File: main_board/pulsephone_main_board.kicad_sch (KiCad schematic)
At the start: 94 parts, among them J1 USB_C_Receptacle_USB2.0_14P, J2 Conn_01x05, J3 Conn_2Rows-35Pins_MountingPin, J4 Conn_2Rows-35Pins_MountingPin, J5 Conn_2Rows-35Pins_MountingPin, J6 Conn_01x01_Socket, J7 Micro_SD_Card_Det1, U1 AP2112K-3.3, U2 PCM5102APWR, U4 TPS63020DSJR/3.7V Reg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

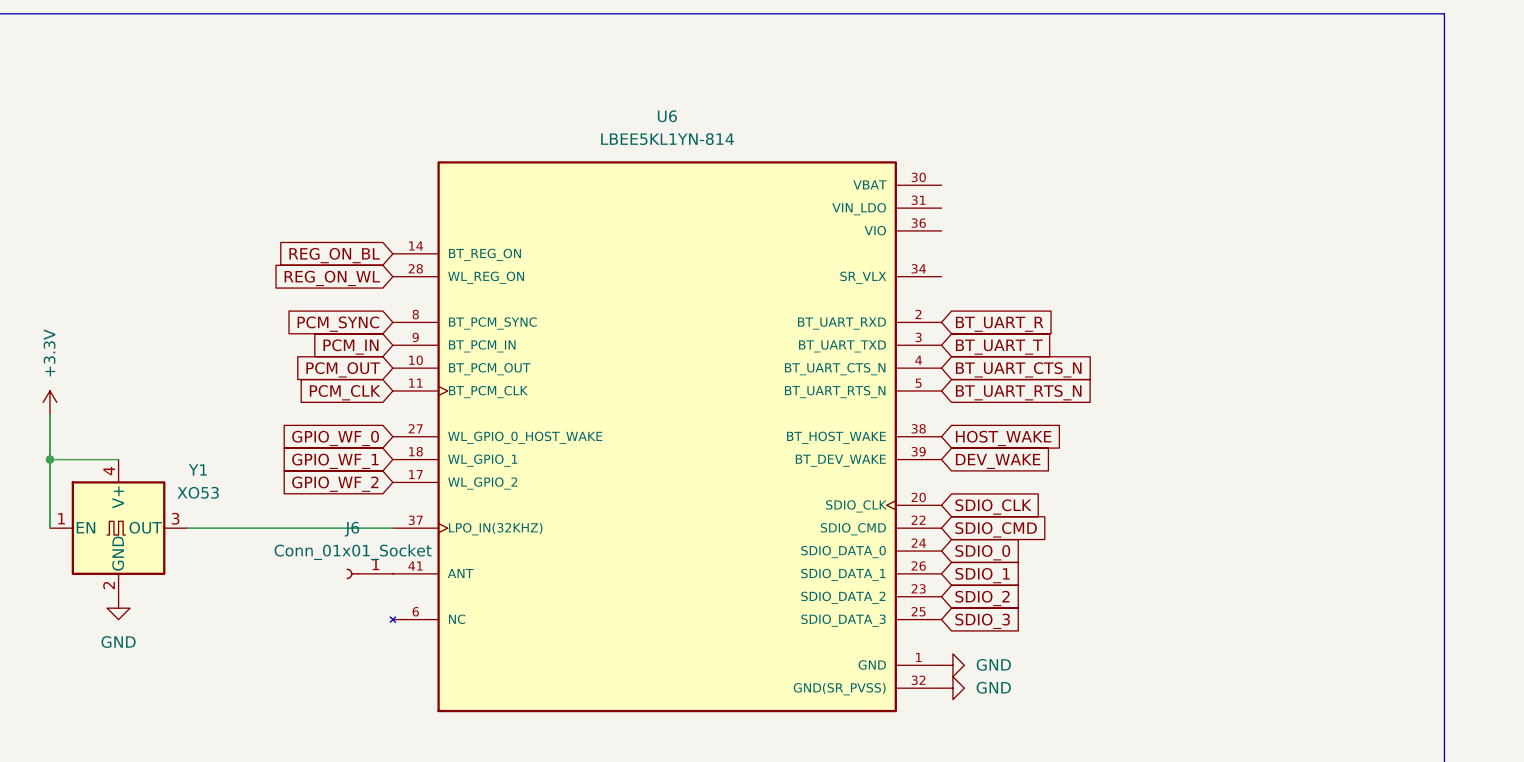
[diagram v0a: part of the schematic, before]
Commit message: Rev2: fix LBEE5KL1YN power pins, SR_VLX inductor, Y1 LPO_IN wiring, DRC constraints
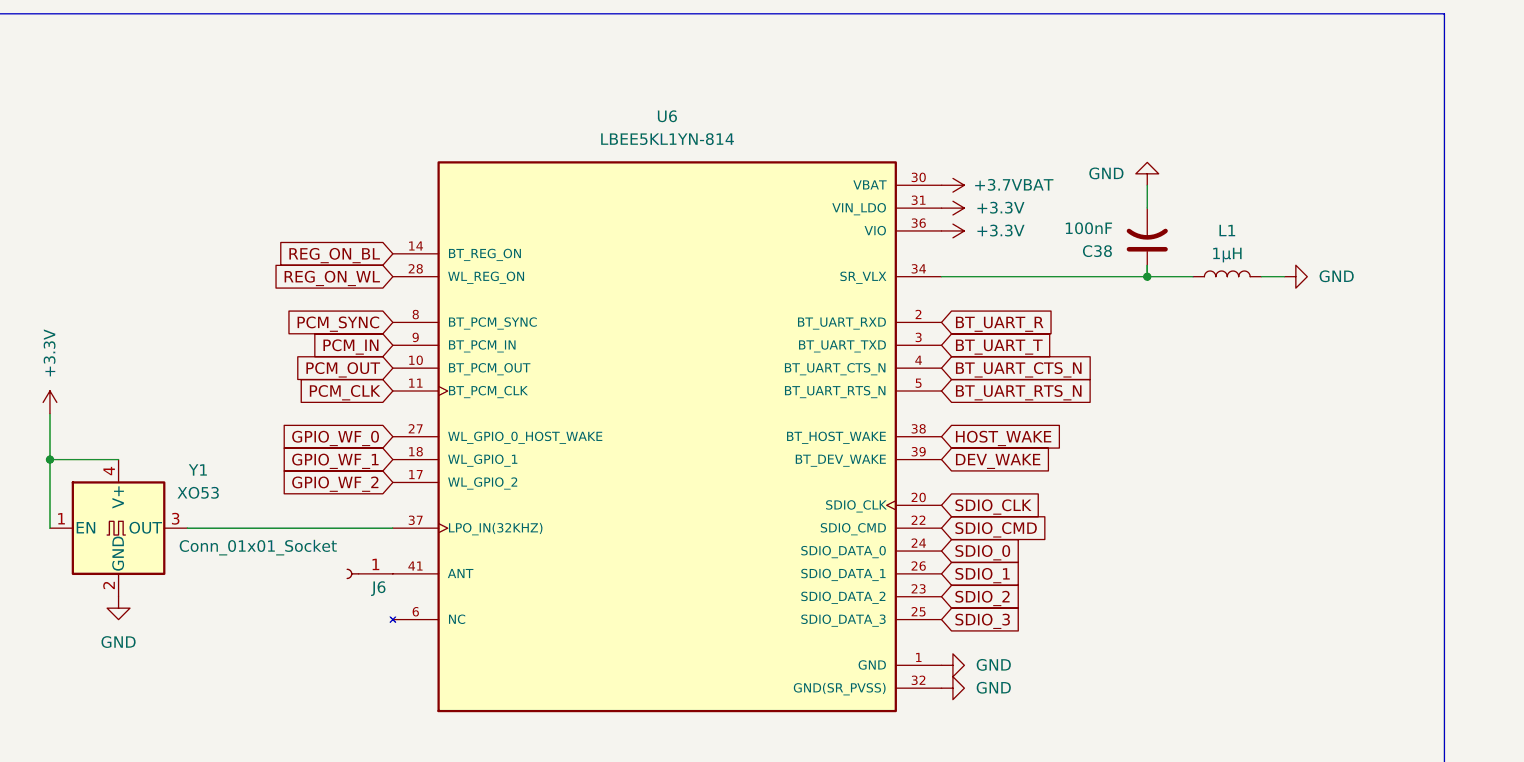
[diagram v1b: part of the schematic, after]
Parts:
- added C38: 100nF, Capacitor_SMD:C_0805_2012Metric, symbol Device:C_US
- added L1: 1µH, Inductor_SMD:L_01005_0402Metric, symbol Device:L
- U3: value ~ -> (none)
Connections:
- net +3.3V: now also U6.31 (VIN_LDO), U6.36 (VIO)
- net +3.7VBAT: now also U6.30 (VBAT)
- net GND: now also C38.2, L1.2
- net at U6.34 (SR_VLX): now also C38.1, L1.1

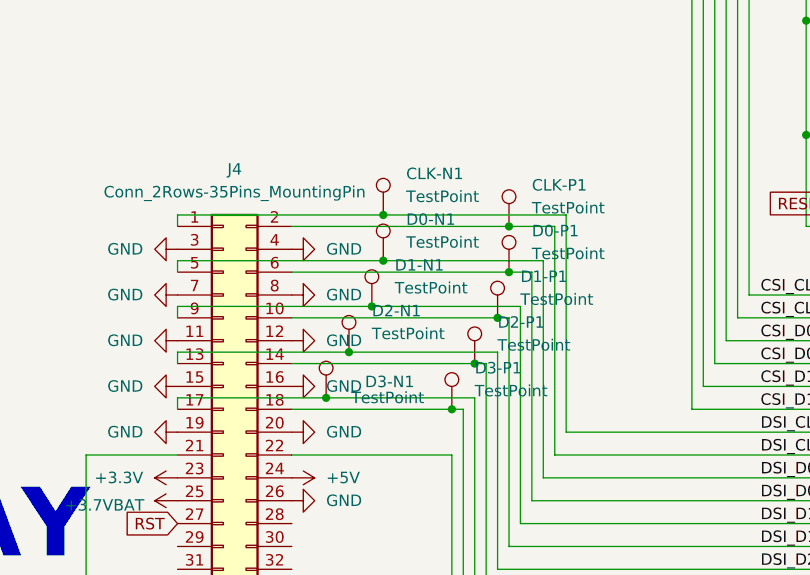
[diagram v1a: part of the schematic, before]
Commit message: Rev2: GND copper pour, reroute, power trace widths
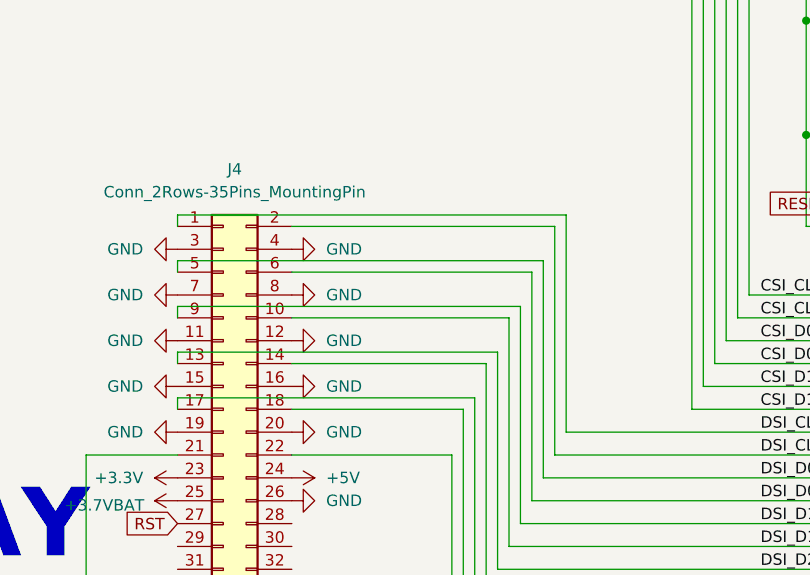
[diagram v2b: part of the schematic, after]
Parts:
- removed CLK-N1, CLK-P1, D0-N1, D0-P1, D1-N1, D1-P1, D2-N1, D2-P1, D3-N1, D3-P1: TestPoint, TestPoint:TestPoint_Pad_D2.5mm, symbol Connector:TestPoint

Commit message: new WIP mod port (new connector for additional modules to further modify the phone
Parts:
- added F1, F2: PPTC, symbol Device:Polyfuse_Small
- added J8: Conn_2Rows-35Pins_MountingPin, DF40-34P:HIROSE_DF40C-34DS-0.4V_58_, symbol Connector_Generic_MountingPin:Conn_2Rows-35Pins_MountingPin
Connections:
- net +3.3V: now also F1.1
- net +3.7VBAT: now also F2.2
- net GND: now also J8.1 (Pin_1), J8.2 (Pin_2), J8.31 (Pin_31), J8.32 (Pin_32), J8.33 (Pin_33), J8.34 (Pin_34)
- new net: F1.2, J8.3 (Pin_3)
- new net: F2.1, J8.4 (Pin_4)
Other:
- note added: "MOD PORT"
- moved on the sheet: 3.3V1, 5V1, BT1, C1, C10, C11, C12, C13, C33, C34, C35, C36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

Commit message: new modport addition to pcb -- 3 unconnected pins, WIP
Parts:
- F1, F2: footprint (none) -> Resistor_SMD:R_0805_2012Metric
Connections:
- net BT_UART_R: now also MCM93_MOD1.103 (33); no longer MCM93_MOD1.102 (32)
- net BT_UART_T: now also MCM93_MOD1.102 (32); no longer MCM93_MOD1.103 (33)
- net CSI_D0_N: now also J3.6 (Pin_6); no longer J3.5 (Pin_5)
- net CSI_D0_P: now also J3.5 (Pin_5); no longer J3.6 (Pin_6)
- net CSI_D1_N: now also J3.10 (Pin_10); no longer J3.9 (Pin_9)
- net CSI_D1_P: now also J3.9 (Pin_9); no longer J3.10 (Pin_10)
- net MOD_GPIO_95: now reaches MCM93_MOD1.95 (25)
- net MOD_GPIO_95: now also J8.13 (Pin_13)
- net MOD_GPIO_96: now reaches MCM93_MOD1.96 (26)
- net MOD_GPIO_96: now also J8.14 (Pin_14)
- net MOD_GPIO_99: now reaches MCM93_MOD1.99 (29)
- net MOD_GPIO_99: now also J8.15 (Pin_15)
- net MOD_UART6_RTS: now reaches MCM93_MOD1.106 (1)
- net MOD_UART6_RTS: now also J8.7 (Pin_7)
- net MOD_UART6_CTS: now reaches MCM93_MOD1.107 (2)
- net MOD_UART6_CTS: now also J8.8 (Pin_8)
- net MOD_GPIO_115: now reaches MCM93_MOD1.115 (10)
- net MOD_GPIO_115: now also J8.16 (Pin_16)
- net MOD_GPIO_116: now reaches MCM93_MOD1.116 (11)
- net MOD_GPIO_116: now also J8.17 (Pin_17)
- net MOD_GPIO_117: now reaches MCM93_MOD1.117 (12)
- net MOD_GPIO_117: now also J8.18 (Pin_18)
- net MOD_GPIO_118: now reaches MCM93_MOD1.118 (13)
- net MOD_GPIO_118: now also J8.19 (Pin_19)
- net MOD_GPIO_119: now reaches MCM93_MOD1.119 (14)
- net MOD_GPIO_119: now also J8.20 (Pin_20)
- net MOD_GPIO_120: now reaches MCM93_MOD1.120 (15)
- net MOD_GPIO_120: now also J8.21 (Pin_21)
- net MOD_I2C7_SCL: now reaches MCM93_MOD1.121 (16)
- net MOD_I2C7_SCL: now also J8.9 (Pin_9)
- net MOD_I2C8_SDA: now reaches MCM93_MOD1.122 (17)
- net MOD_I2C8_SDA: now also J8.10 (Pin_10)
- net MOD_I2C8_SCL: now reaches MCM93_MOD1.123 (18)
- net MOD_I2C8_SCL: now also J8.11 (Pin_11)
- net MOD_UART6_RX: now reaches MCM93_MOD1.124 (19)
- net MOD_UART6_RX: now also J8.5 (Pin_5)
- net MOD_UART6_TX: now reaches MCM93_MOD1.125 (20)
- net MOD_UART6_TX: now also J8.6 (Pin_6)
- net MOD_GPIO_128: now reaches MCM93_MOD1.128 (23)
- net MOD_GPIO_128: now also J8.22 (Pin_22)
- net MOD_GPIO_130: now reaches MCM93_MOD1.130 (25)
- net MOD_GPIO_130: now also J8.23 (Pin_23)
- net MOD_GPIO_48: now reaches J8.12 (Pin_12)
- net MOD_GPIO_48: now also MCM93_MOD1.48 (13)

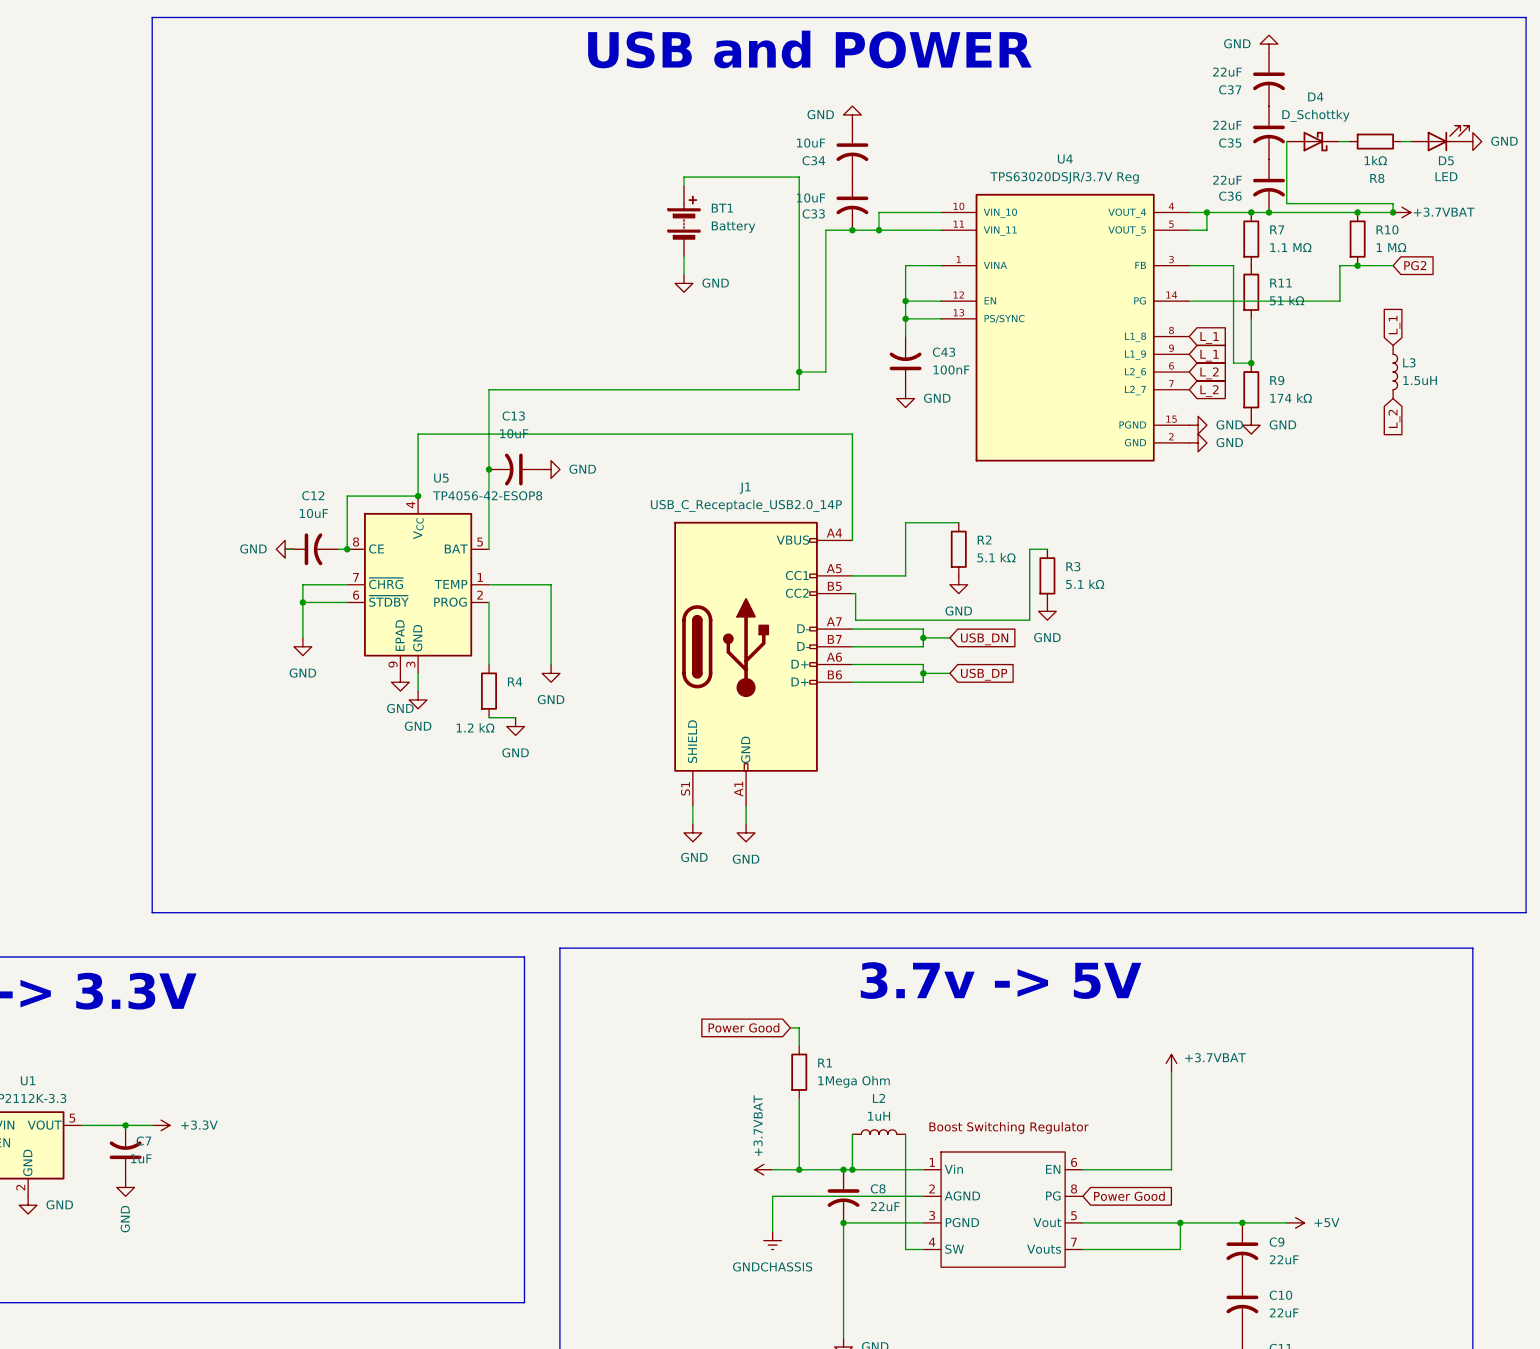
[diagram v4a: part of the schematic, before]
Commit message: add power good leds to 5v and 3v3.
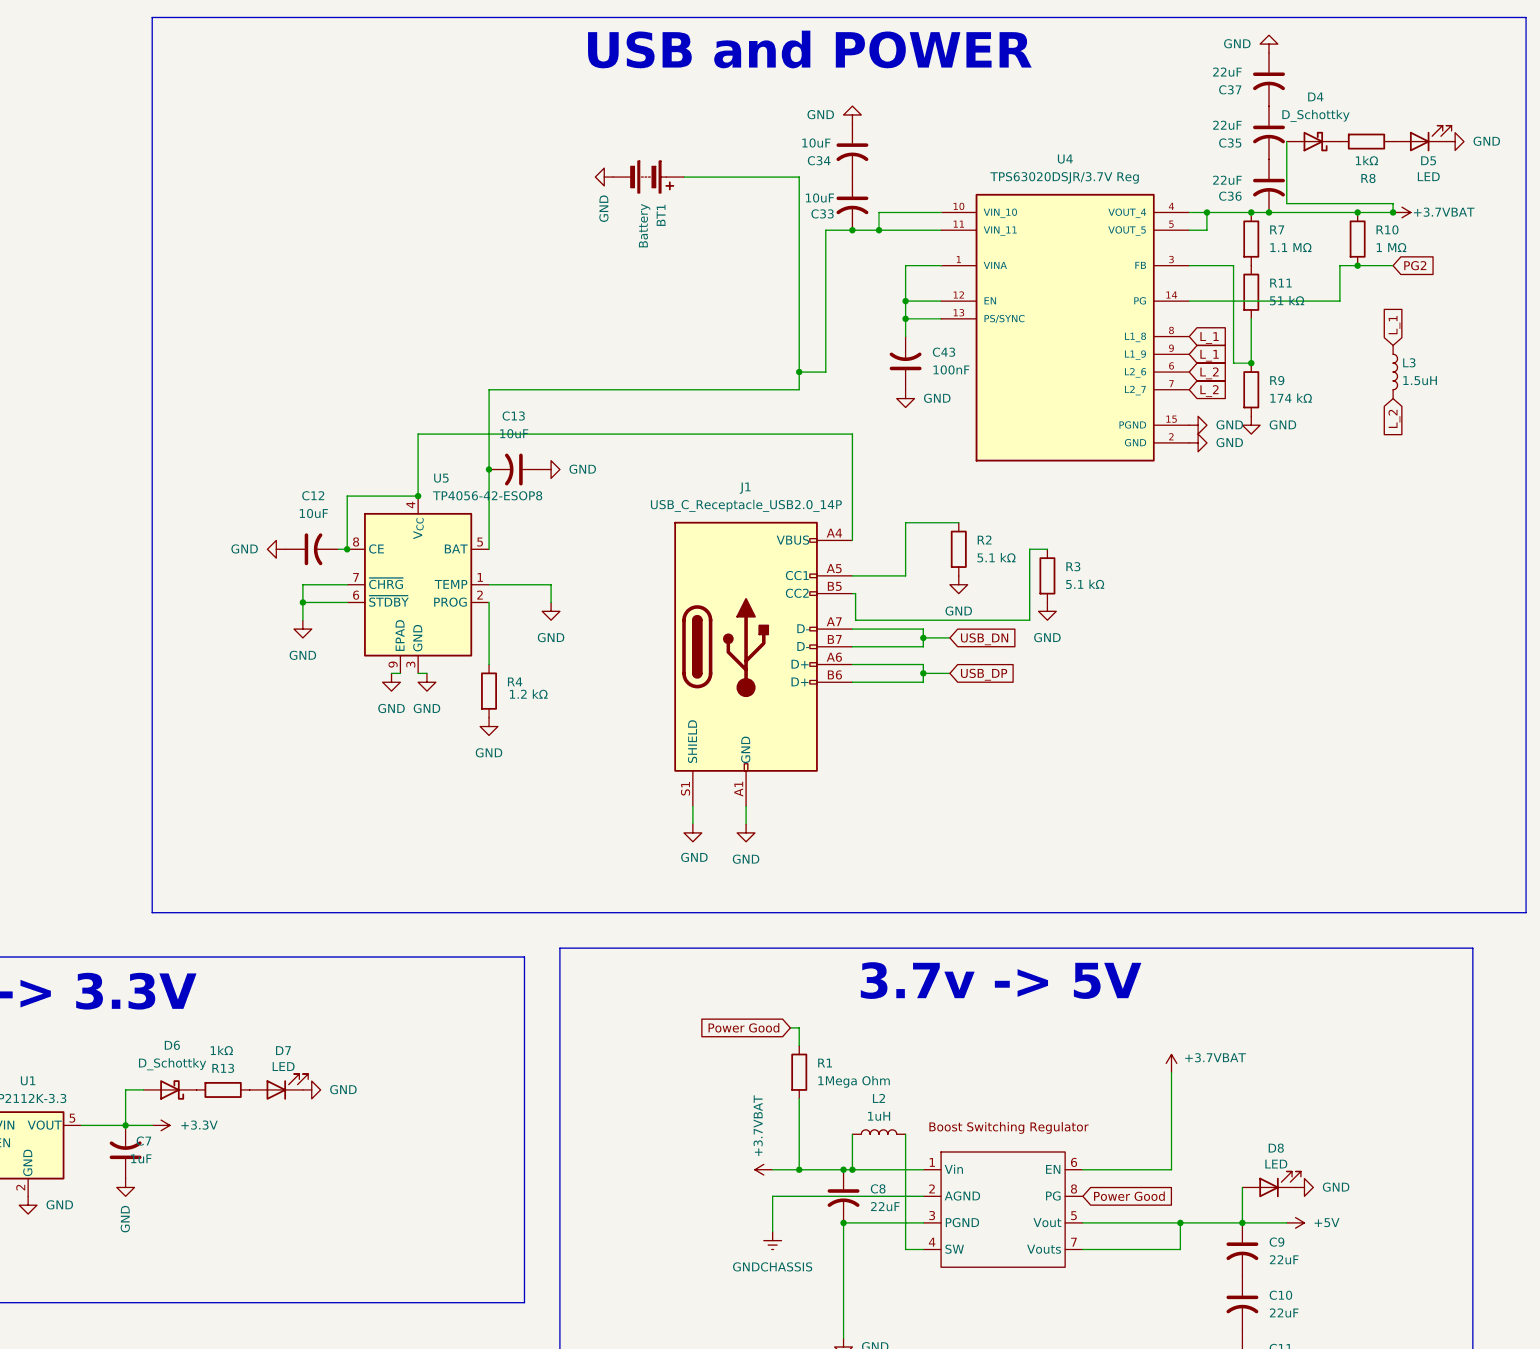
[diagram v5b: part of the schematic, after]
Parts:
- added D6: D_Schottky, Diode_SMD:D_SMA, symbol Device:D_Schottky
- added D7, D8: LED, LED_SMD:LED_0805_2012Metric, symbol Device:LED
- added R13: 1kΩ, Resistor_SMD:R_0805_2012Metric, symbol Device:R
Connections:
- net +3.3V: now also D6.2 (A)
- net +5V: now also D8.2 (A)
- net GND: now also D7.1 (K), D8.1 (K)
- new net: D7.2 (A), R13.1
- new net: D6.1 (K), R13.2
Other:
- moved on the sheet: BT1, D5, R8
